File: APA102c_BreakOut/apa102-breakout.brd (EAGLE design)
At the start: 76.8 x 51.4 mm, 52 parts

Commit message: updated routing again
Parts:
- moved C12 0.52 mm to (28.2, 22.5)
- moved C24 0.38 mm to (53.2, 2.26)
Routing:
- net VCC: track 0.00 -> 494.1 mm
- net GND: track 0.00 -> 291.1 mm
- net N$61: track 0.00 -> 15.5 mm
- net N$41: track 0.00 -> 15.5 mm
- net N$62: track 0.00 -> 11.7 mm
- net N$42: track 0.00 -> 11.7 mm
- net CLK: track 0.00 -> 11.7 mm
- net N$73: track 0.00 -> 11.6 mm
- net N$51: track 0.00 -> 11.6 mm
- net DATA: track 0.00 -> 11.3 mm
- net N$71: track 0.00 -> 8.58 mm
- net N$50: track 0.00 -> 8.58 mm
- net N$64: track 0.00 -> 8.57 mm
- net N$43: track 0.00 -> 8.57 mm
- net N$69: track 0.00 -> 8.57 mm
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
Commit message: added silk screen
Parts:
- moved U$1 2.00 mm to (6.22, 5.68)
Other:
- board size 76.8 x 51.4 mm -> 76 x 51 mm
- board text added: "CLK"
- board text added: "DATA"
- board text added: "GND"
- board text added: "VCC"

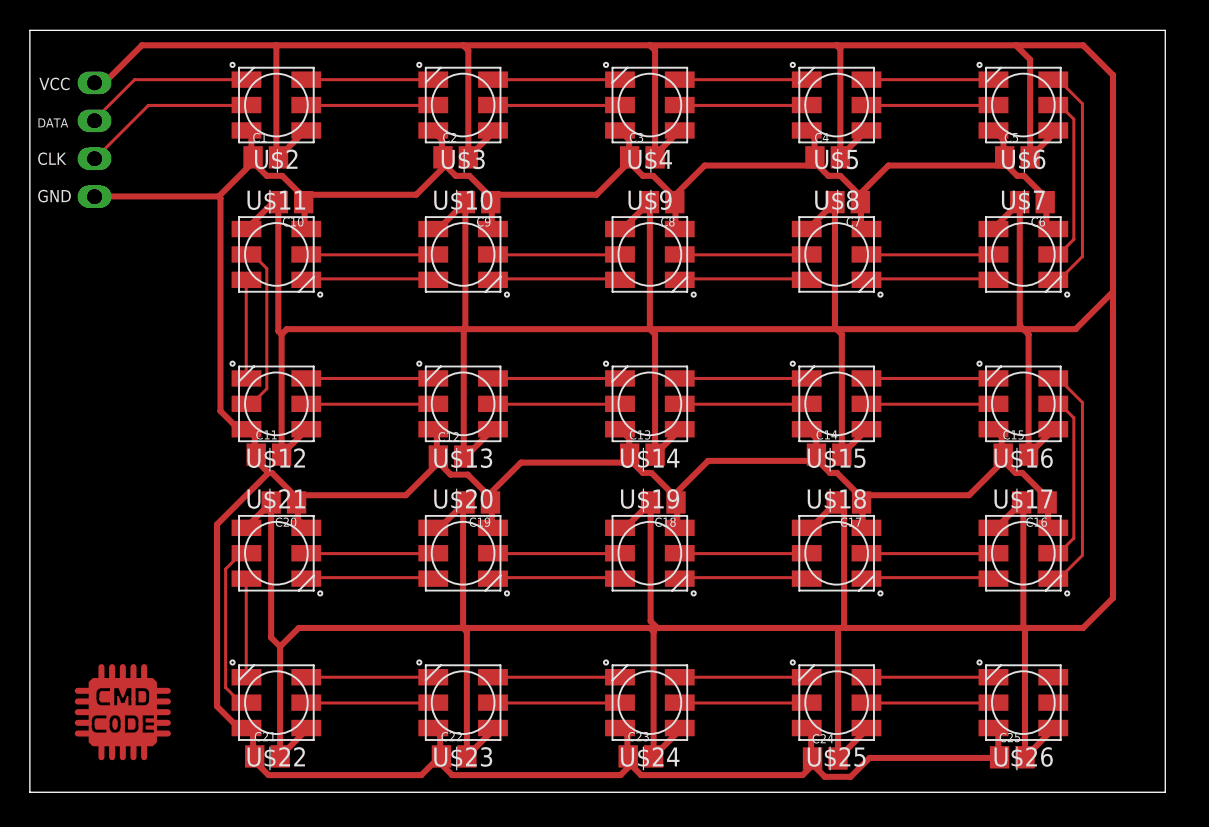
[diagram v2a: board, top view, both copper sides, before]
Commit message: adding breakout board for stm32g031
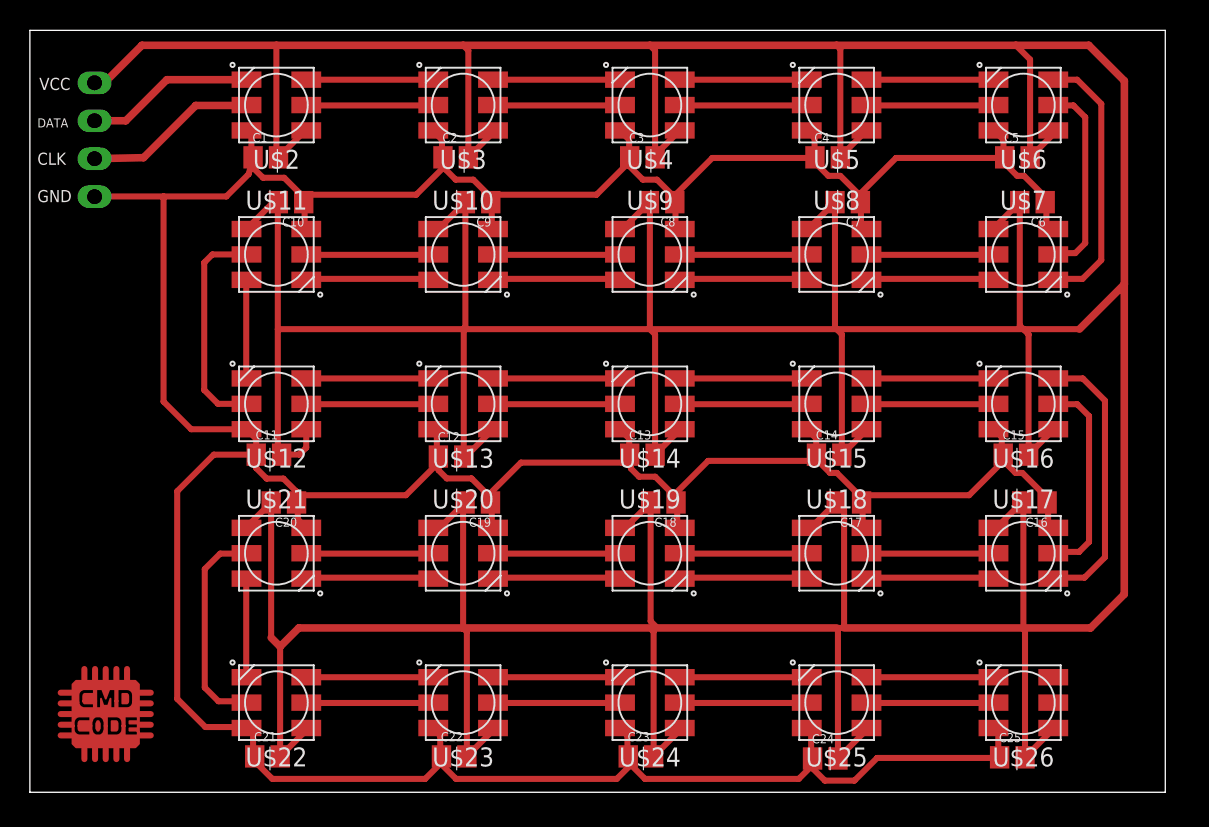
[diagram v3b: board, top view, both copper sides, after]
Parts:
- moved U$1 1.15 mm to (5.08, 5.55)
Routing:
- net GND: track 291.1 -> 303.1 mm
- net N$51: track 11.6 -> 14.8 mm
- net N$61: track 15.5 -> 18.7 mm
- net VCC: track 494.1 -> 497.0 mm
- net N$73: track 11.6 -> 14.4 mm
- net N$41: track 15.5 -> 18.1 mm
- net N$62: track 11.7 -> 13.9 mm
- net N$42: track 11.7 -> 13.4 mm
